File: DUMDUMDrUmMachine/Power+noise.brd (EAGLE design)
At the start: 100 x 80 mm, 58 parts, among them IC1 TL072P, IC4 7815T, IC6 4584N, IC7 7805T, X1 5 VDC, X2 15 VAC, X3 NOISE_OUT

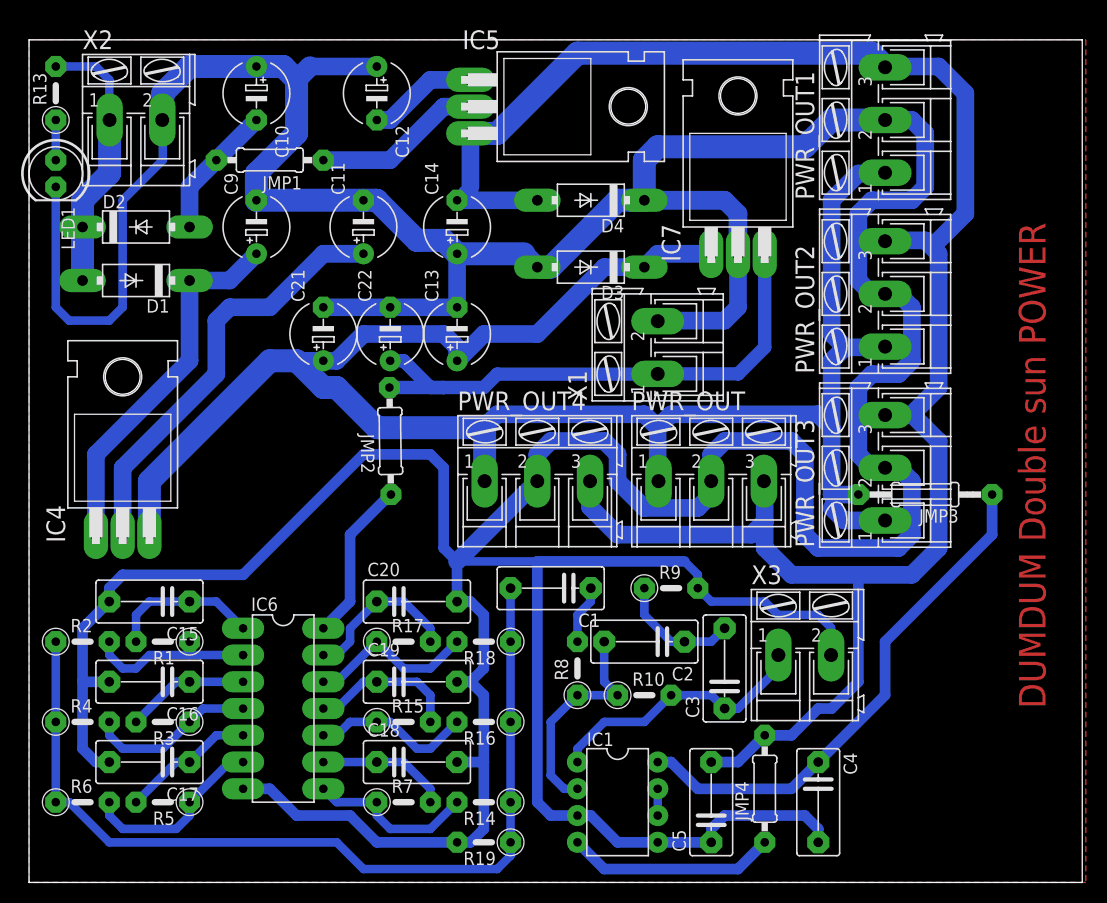
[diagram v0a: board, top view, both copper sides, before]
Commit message: 7seg-pcb should be finnished, also changed text in power-pcb
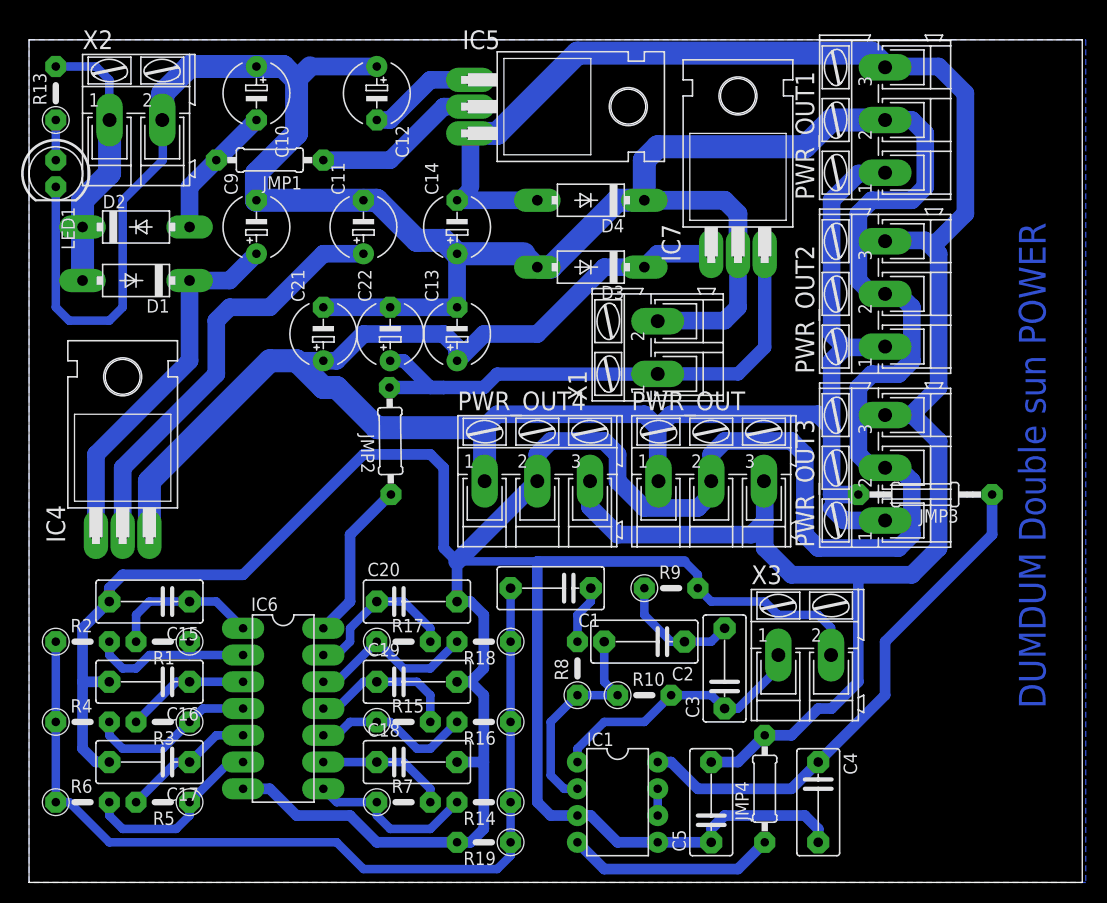
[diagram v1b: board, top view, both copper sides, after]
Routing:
- added copper zone on layer 16, net GND
- removed copper zone on layer 1, net GND
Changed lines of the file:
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@@
 <wire x1="100" y1="80" x2="0" y2="80" width="0" layer="20"/>
 <wire x1="0" y1="80" x2="0" y2="0" width="0" layer="20"/>
-<text x="96.52" y="16.51" size="2.54" layer="1" rot="R90">DUMDUM Double sun POWER</text>
+<text x="96.52" y="16.51" size="2.54" layer="16" rot="R90">DUMDUM Double sun POWER</text>
 </plain>
 <attributes>
@@
 </class>
 </classes>
-<designrules name="hobby">
+<designrules name="hobby-desingrules">
 <description language="sv">&lt;b&gt;EAGLE Design Rules&lt;/b&gt;
 &lt;p&gt;
@@
 <wire x1="59.7408" y1="53.34" x2="59.69" y2="53.2892" width="1.27" layer="16"/>
 <wire x1="59.69" y1="3.81" x2="64.77" y2="3.81" width="1.016" layer="16"/>
-<polygon width="0.4064" layer="1">
+<polygon width="0.4064" layer="16">
 <vertex x="0" y="80.01"/>
 <vertex x="100.33" y="80.01"/>
